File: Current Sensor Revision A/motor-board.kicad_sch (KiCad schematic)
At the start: 19 parts, among them J1 SMA, J3 Screw_Terminal_01x02, U1 ACS37030, U2 MCP633

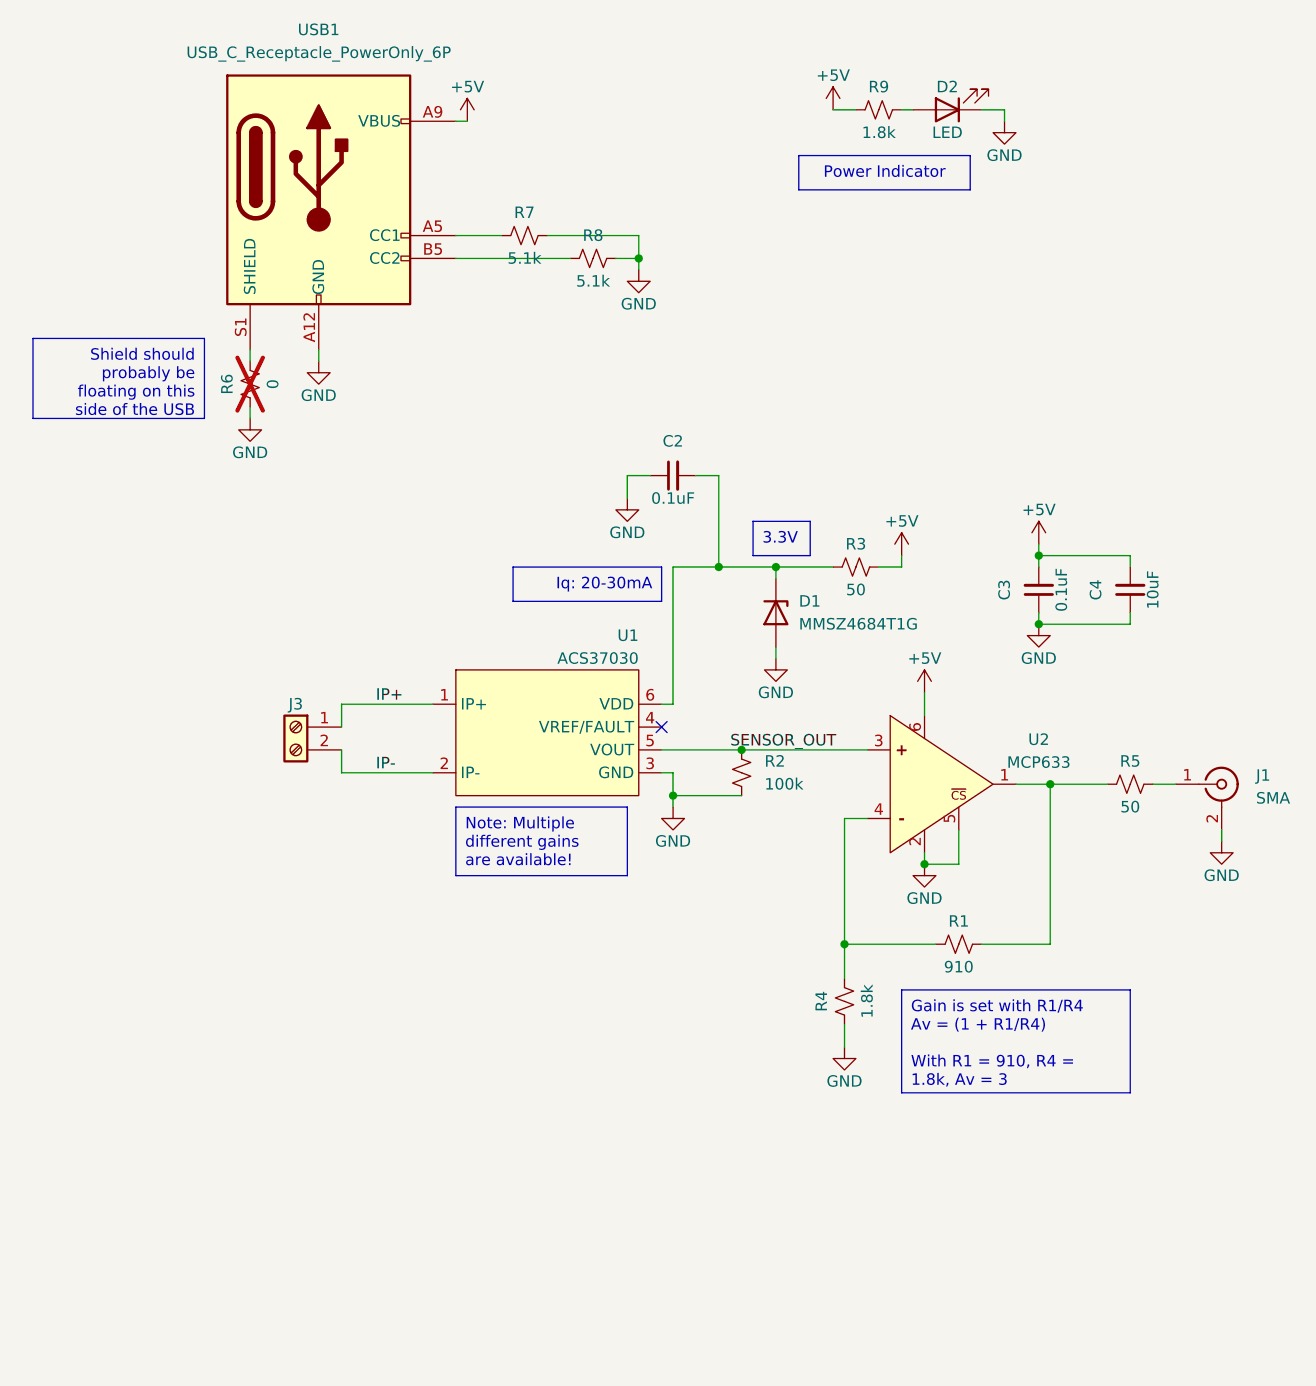
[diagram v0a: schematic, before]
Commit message: Added A2/A3 PCB files and 3D Board Render
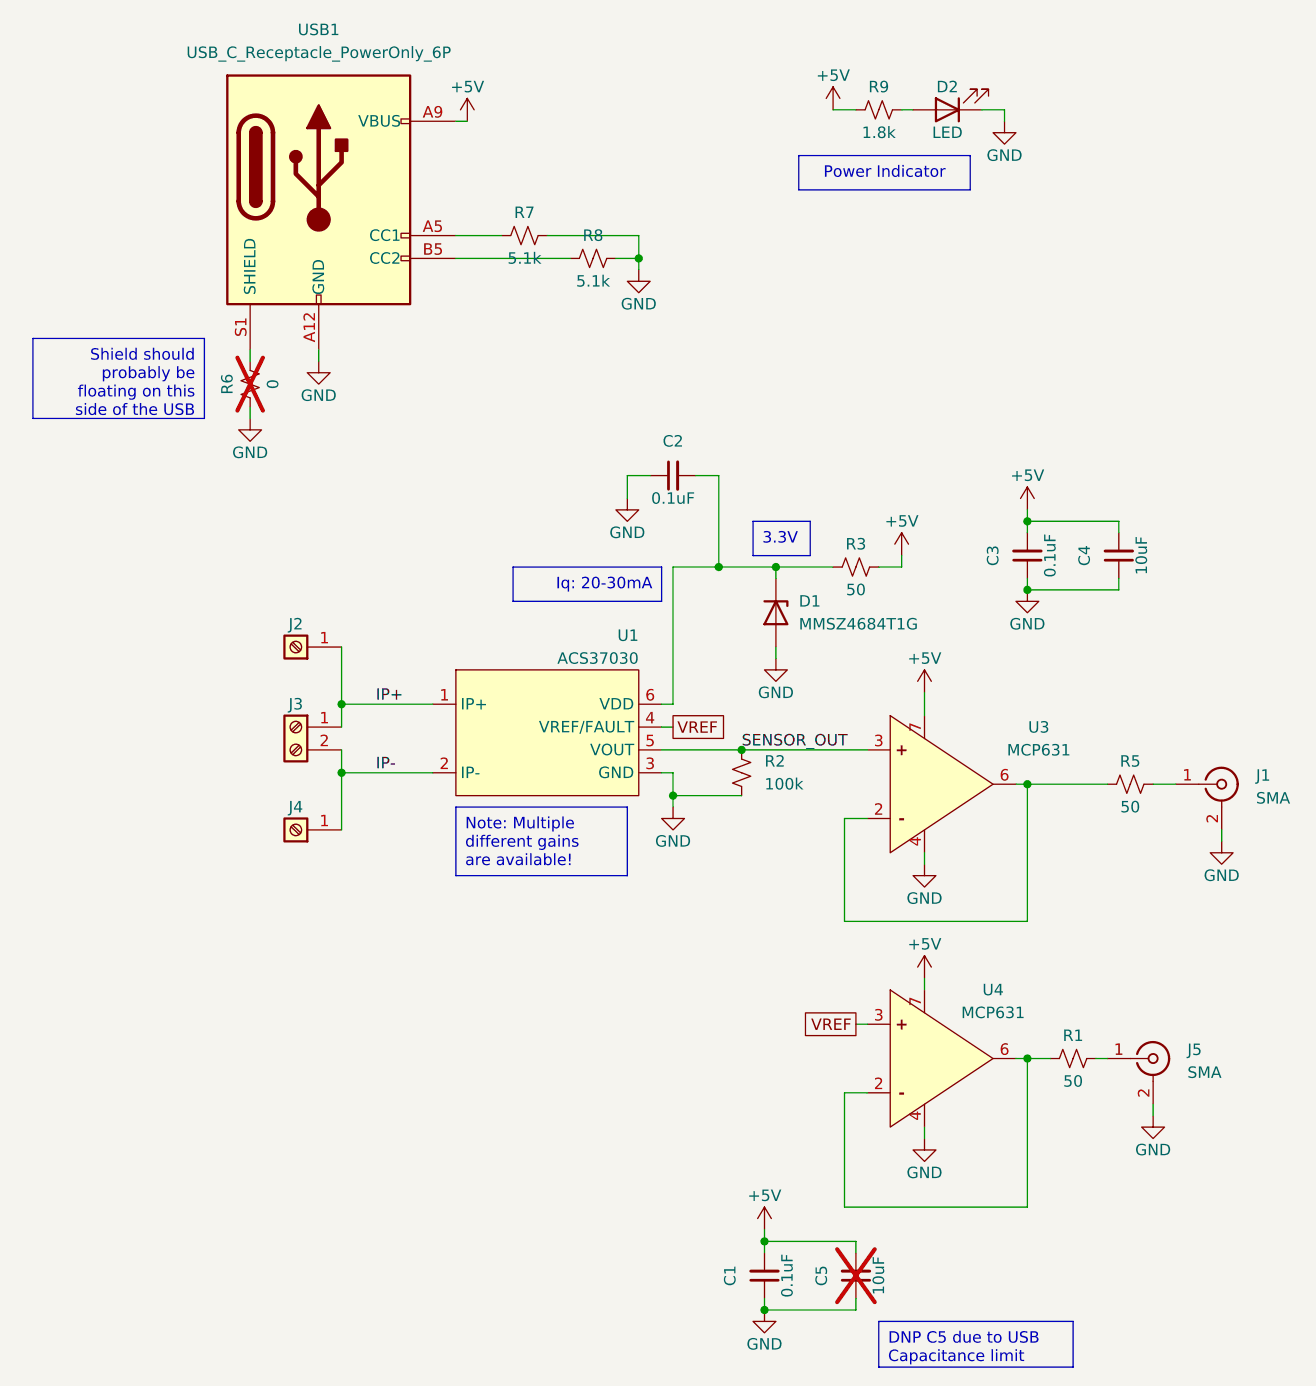
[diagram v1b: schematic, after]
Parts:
- removed R4: 1.8k, Resistor_SMD:R_0805_2012Metric_Pad1.20x1.40mm_HandSolder, symbol Device:R_Small_US
- removed U2: MCP633, StandardPackages_Custom:SOT23-6, symbol Current Sensor Sch Library:MCP633
- added C1: 0.1uF, Capacitor_SMD:C_0805_2012Metric_Pad1.18x1.45mm_HandSolder, symbol Device:C_Small
- added C5: 10uF, Capacitor_SMD:C_0805_2012Metric_Pad1.18x1.45mm_HandSolder, symbol Device:C_Small
- added J2, J4: 74650094R, Current Sensor PCB Library:74650094R, symbol Connector:Screw_Terminal_01x01
- added J5: SMA, Current Sensor PCB Library:CONSMA002-L-G, symbol Connector:Conn_Coaxial
- added U3, U4: MCP631, StandardPackages_Custom:SOIC-8, symbol Current Sensor Sch Library:MCP631
- R1: value 910 -> 50; footprint Resistor_SMD:R_0805_2012Metric_Pad1.20x1.40mm_HandSolder -> Resistor_SMD:R_1206_3216Metric_Pad1.30x1.75mm_HandSolder
- R3, R5: footprint Resistor_SMD:R_0805_2012Metric_Pad1.20x1.40mm_HandSolder -> Resistor_SMD:R_1206_3216Metric_Pad1.30x1.75mm_HandSolder
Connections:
- net +5V: now also C1.2, C5.2, U3.7 (VDD), U4.7 (VDD)
- net GND: now also C1.1, C5.1, J5.2 (Ext), U3.4 (VSS), U4.4 (VSS)
- net IP+: now also J2.1 (Pin_1)
- net IP-: now also J4.1 (Pin_1)
- net SENSOR_OUT: now also U3.3 (IN+)
- net at R1.1: now also U4.2 (IN-), U4.6 (VOUT)
- net at R1.2: now also J5.1 (In); no longer R5.1
- net VREF: now reaches U1.4 (VREF/FAULT)
- net VREF: now also U4.3 (IN+)
- new net: R5.1, U3.2 (IN-), U3.6 (VOUT)
- no-connect marks 1 -> 0
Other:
- moved on the sheet: C3, C4
